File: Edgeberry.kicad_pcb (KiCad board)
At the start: 2 copper layers, 135 x 90 mm, 169 parts, among them P1 12Vin, Q1 BC547, Q2 BC547, Q3 BC547, SW1 SW_PUSH, U1 24LC256, U2 LM2596S-5.0

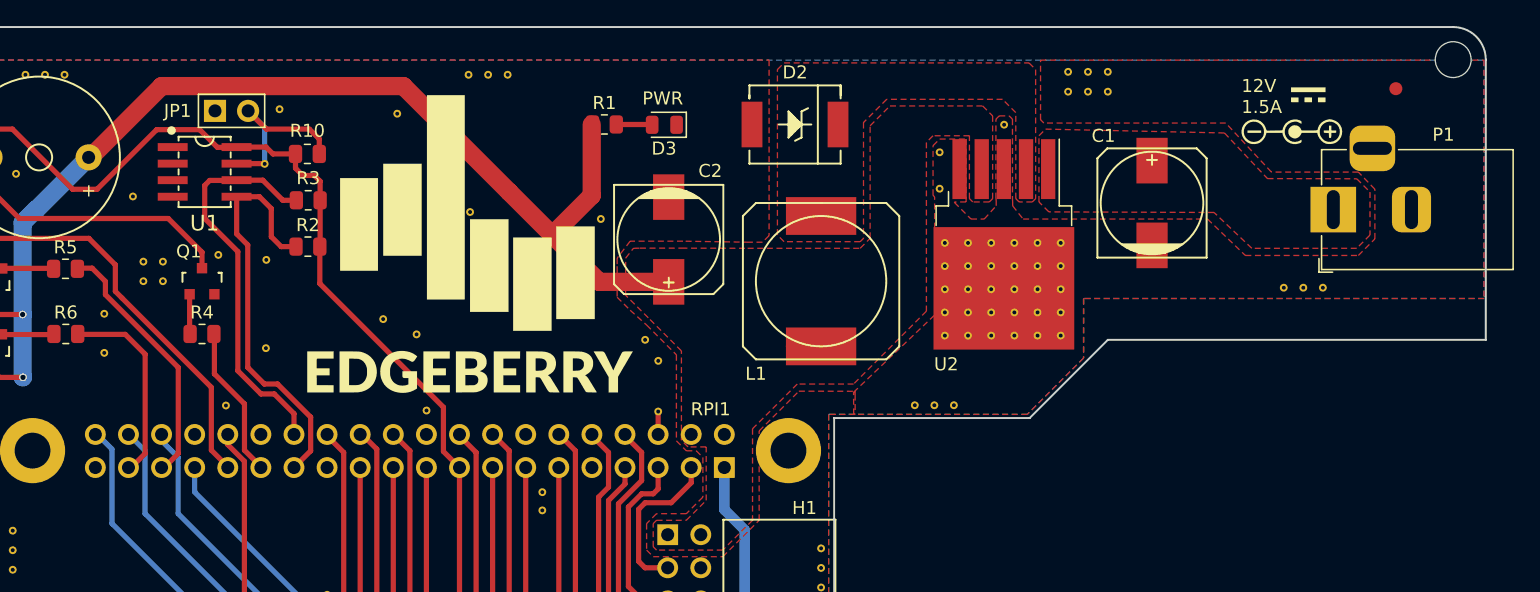
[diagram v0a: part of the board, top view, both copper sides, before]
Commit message: Added a Molex 2Pin header on 12V
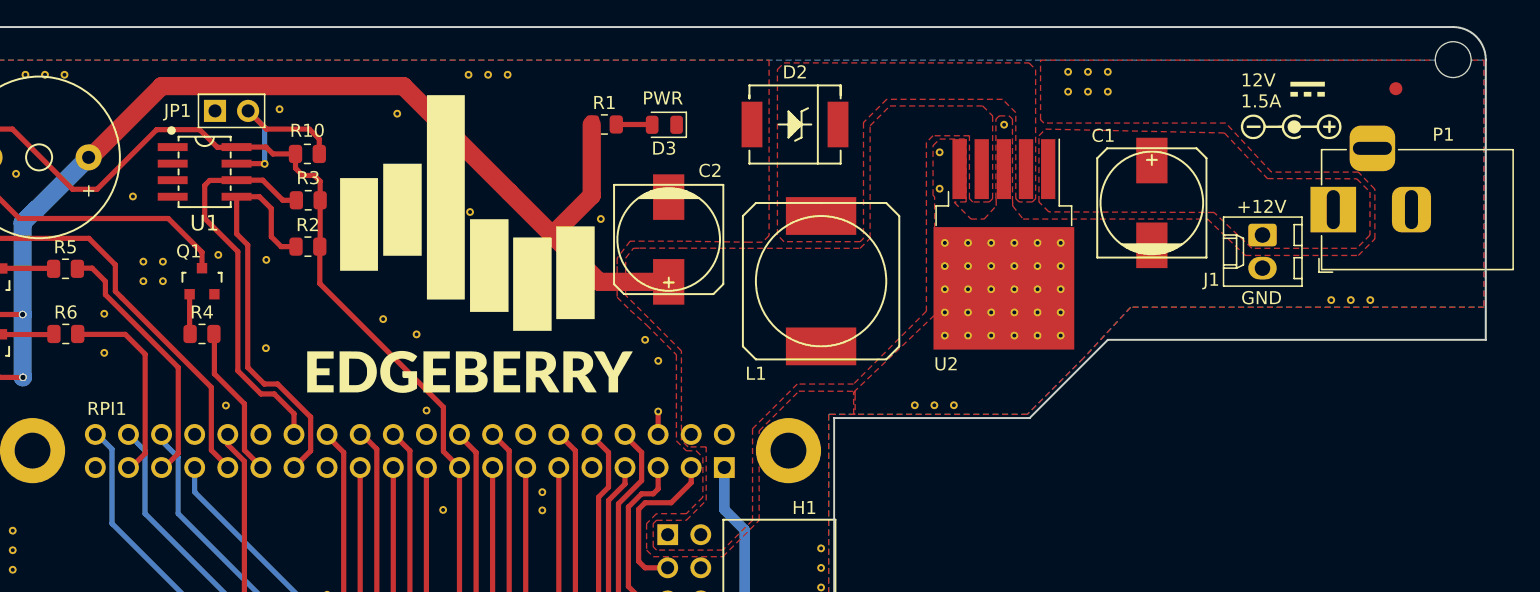
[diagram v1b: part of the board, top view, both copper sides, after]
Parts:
- added J1: Molex_KK_1x02_P2.54mm_CONN, Connector_Molex:Molex_KK-254_AE-6410-02A_1x02_P2.54mm_Vertical, F.Cu at (201.5, 67.7)
- added REF**: via_0.6mm, emcosys:via_0.6mm, B.Cu at (138.6, 88.8)
- H1: value EdgeBerry_IO -> 2X16Pin_2.54mm_Right_Angle_Receptacle_Connector
- P1: value 12Vin -> Barrel_Jack_CONN
- RPI1: value RPi_GPIO -> 2X20Pin_2.54mm_Receptacle_Connector
- moved G*** 4.80 mm to (193.4, 64.0)
- moved REF** 3.76 mm to (209.8, 72.7)
- moved REF** 3.76 mm to (208.3, 72.7)
- moved REF** 3.76 mm to (206.8, 72.7)
- moved G*** 0.43 mm to (204.9, 56.6)
- moved G*** 0.38 mm to (203.7, 59.4)
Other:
- board text added: "+12V"
- board text added: "REV 1.4"
- board text added: "REV.: 1.4, Mid 2024"
- board text removed: "REV 1.3"
- board text removed: "REV.: 1.3, Mid 2024"
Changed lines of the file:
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@@
   (net 43 "Net-(Q3-Pad2)")
   (footprint "Capacitors_SMD:c_elec_8x10" (layer "F.Cu")
-    (at 193.04 65.272 90)
+    (at 193.028 65.2672 90)
     (descr "SMT capacitor, aluminium electrolytic, 8x10")
     (property "Sheetfile" "Edgeberry.kicad_sch")
@@
       (effects (font (size 1 1) (thickness 0.15)))
     )
-    (fp_text value "EdgeBerry_IO" (at 0 -9.351 -90) (layer "F.Fab")
+    (fp_text value "2X16Pin_2.54mm_Right_Angle_Receptacle_Connector" (at 0 -4.85 -90) (layer "F.Fab")
       (effects (font (size 1 1) (thickness 0.15)))
     )
@@
     )
   )
+  (footprint "Connector_Molex:Molex_KK-254_AE-6410-02A_1x02_P2.54mm_Vertical" (layer "F.Cu")
+    (at 201.517 67.731 -90)
+    (descr "Molex KK-254 Interconnect System, old/engineering part number: AE-6410-02A example for new part number: 22-27-2021, 2 Pins (http://www.molex.com/pdm_docs/sd/022272021_sd.pdf), generated with kicad-footprint-generator")
+    (tags "connector Molex KK-254 vertical")
+    (property "Sheetfile" "Edgeberry.kicad_sch")
+    (property "Sheetname" "")
+    (attr through_hole)
+    (fp_text reference "J1" (at 3.429 3.917 180) (layer "F.SilkS")
+      (effects (font (size 1 1) (thickness 0.15)))
+    )
+    (fp_text value "Molex_KK_1x02_P2.54mm_CONN" (at 6.041 -0.02 180) (layer "F.Fab")
+      (effects (font (size 1 1) (thickness 0.15)))
+    )
+    (fp_text user "${REFERENCE}" (at 1.27 -1.732 90) (layer "F.Fab")
+      (effects (font (size 1 1) (thickness 0.15)))
+    )
+    (fp_line (start 3.34 -2.43) (end 3.34 -3.03) (layer "F.SilkS") (width 0.12))
+    (fp_line (start 2.29 1.46) (end 2.54 1.99) (layer "F.SilkS") (width 0.12))
+    (fp_line (start -1.38 2.99) (end 3.92 2.99) (layer "F.SilkS") (width 0.12))
+    (fp_line (start 0.25 1.46) (end 2.29 1.46) (layer "F.SilkS") (width 0.12))
+    (fp_line (start 3.92 2.99) (end 3.92 -3.03) (layer "F.SilkS") (width 0.12))
+    (fp_line (start 1.74 -2.43) (end 3.34 -2.43) (layer "F.SilkS") (width 0.12))
+    (fp_line (start 2.54 1.99) (end 2.54 2.99) (layer "F.SilkS") (width 0.12))
+    (fp_line (start 0 1.99) (end 2.54 1.99) (layer "F.SilkS") (width 0.12))
+    (fp_line (start 2.29 2.99) (end 2.29 1.99) (layer "F.SilkS") (width 0.12))
+    (fp_line (start 0.25 2.99) (end 0.25 1.99) (layer "F.SilkS") (width 0.12))
+    (fp_line (start 3.92 -3.03) (end -1.38 -3.03) (layer "F.SilkS") (width 0.12))
+    (fp_line (start -0.8 -2.43) (end 0.8 -2.43) (layer "F.SilkS") (width 0.12))
+    (fp_line (start 0 1.99) (end 0.25 1.46) (layer "F.SilkS") (width 0.12))
+    (fp_line (start 0 2.99) (end 0 1.99) (layer "F.SilkS") (width 0.12))
+    (fp_line (start 0.8 -2.43) (end 0.8 -3.03) (layer "F.SilkS") (width 0.12))
+    (fp_line (start -1.38 -3.03) (end -1.38 2.99) (layer "F.SilkS") (width 0.12))
+    (fp_line (start -0.8 -3.03) (end -0.8 -2.43) (layer "F.SilkS") (width 0.12))
+    (fp_line (start 1.74 -3.03) (end 1.74 -2.43) (layer "F.SilkS") (width 0.12))
+    (fp_line (start -1.77 -3.42) (end -1.77 3.38) (layer "F.CrtYd") (width 0.05))
+    (fp_line (start 4.31 -3.42) (end -1.77 -3.42) (layer "F.CrtYd") (width 0.05))
+    (fp_line (start 4.31 3.38) (end 4.31 -3.42) (layer "F.CrtYd") (width 0.05))
+    (fp_line (start -1.77 3.38) (end 4.31 3.38) (layer "F.CrtYd") (width 0.05))
+    (fp_line (start 3.81 -2.92) (end -1.27 -2.92) (layer "F.Fab") (width 0.1))
+    (fp_line (start -1.27 -0.5) (end -0.562893 0) (layer "F.Fab") (width 0.1))
+    (fp_line (start -0.562893 0) (end -1.27 0.5) (layer "F.Fab") (width 0.1))
+    (fp_line (start -1.27 -2.92) (end -1.27 2.88) (layer "F.Fab") (width 0.1))
+    (fp_line (start -1.27 2.88) (end 3.81 2.88) (layer "F.Fab") (width 0.1))
+    (fp_line (start 3.81 2.88) (end 3.81 -2.92) (layer "F.Fab") (width 0.1))
+    (pad "1" thru_hole roundrect (at 0 0 270) (size 1.74 2.19) (drill 1.19) (layers *.Cu *.Mask) (roundrect_rratio 0.143678)
+      (net 6 "+12V") (pinfunction "Pin_1") (pintype "passive"))
+    (pad "2" thru_hole oval (at 2.54 0 270) (size 1.74 2.19) (drill 1.19) (layers *.Cu *.Mask)
+      (net 2 "GND") (pinfunction "Pin_2") (pintype "passive"))
+    (model "${KICAD6_3DMODEL_DIR}/Connector_Molex.3dshapes/Molex_KK-254_AE-6410-02A_1x02_P2.54mm_Vertical.wrl"
+      (offset (xyz 0 0 -1))
+      (scale (xyz 1 1 1))
+      (rotate (xyz 0 0 90))
+    )
+    (model "/home/tom/Projects/KiCad_library/3D models/molex_kk_2.54mm_(0.1inch)_latching_2way_vertical_header.step"
+      (offset (xyz 1.2 0 1.5))
+      (scale (xyz 1 1 1))
+      (rotate (xyz -90 0 180))
+    )
+  )
   (footprint "Resistor_SMD:R_0805_2012Metric" (layer "F.Cu")
     (at 128.274 68.62 180)
@@
   )
   (footprint "LOGO" (layer "F.Cu")
-    (at 203.8 59.8)
+    (at 203.749 59.422)
     (attr board_only exclude_from_pos_files exclude_from_bom)
     (fp_text reference "G***" (at 0 0) (layer "F.SilkS") hide
@@
   )
   (footprint "LOGO" (layer "F.Cu")
-    (at 205 57)
+    (at 204.949 56.572)
     (attr board_only exclude_from_pos_files exclude_from_bom)
     (fp_text reference "G***" (at 0 0) (layer "F.SilkS") hide
@@
       (effects (font (size 1 1) (thickness 0.15)))
     )
-    (fp_text value "12Vin" (at -6.2 -5.5) (layer "F.Fab")
+    (fp_text value "Barrel_Jack_CONN" (at -6.45 -3.6425) (layer "F.Fab")
       (effects (font (size 1 1) (thickness 0.15)))
     )
-    (fp_text user "${REFERENCE}" (at -3 -2.95) (layer "F.Fab")
+    (fp_text user "${REFERENCE}" (at -2.95 -2.2425) (layer "F.Fab")
       (effects (font (size 1 1) (thickness 0.15)))
     )
@@
     (property "Sheetname" "")
     (attr through_hole)
-    (fp_text reference "RPI1" (at -23.0786 3.2035 180) (layer "F.SilkS")
+    (fp_text reference "RPI1" (at 23.2464 3.2285 180) (layer "F.SilkS")
       (effects (font (size 1 1) (thickness 0.15)))
     )
-    (fp_text value "RPi_GPIO" (at -1.9546 -3.1495 180) (layer "F.Fab")
+    (fp_text value "2X20Pin_2.54mm_Receptacle_Connector" (at -1.9546 -3.1495 180) (layer "F.Fab")
       (effects (font (size 1 1) (thickness 0.15)))
     )
@@
   )
   (footprint "emcosys:via_0.6mm" (layer "B.Cu")
-    (at 206.149 71.772 -90)
+    (at 209.792 72.722 -90)
     (attr through_hole)
     (fp_text reference "REF**" (at 0 -0.9525 -90) (layer "B.SilkS") hide
@@
   )
   (footprint "emcosys:via_0.6mm" (layer "B.Cu")
-    (at 204.649 71.772 -90)
+    (at 208.292 72.722 -90)
     (attr through_hole)
     (fp_text reference "REF**" (at 0 -0.9525 -90) (layer "B.SilkS") hide
@@
   )
   (footprint "emcosys:via_0.6mm" (layer "B.Cu")
-    (at 203.149 71.772 -90)
+    (at 206.792 72.722 -90)
     (attr through_hole)
     (fp_text reference "REF**" (at 0 -0.9525 -90) (layer "B.SilkS") hide
@@
   )
   (footprint "emcosys:via_0.6mm" (layer "B.Cu")
+    (at 138.649 88.822 -90)
+    (attr through_hole)
+    (fp_text reference "REF**" (at 0 -0.9525 -90) (layer "B.SilkS") hide
+      (effects (font (size 1 1) (thickness 0.15)) (justify mirror))
+    )
+    (fp_text value "via_0.6mm" (at 0 1.0795 -90) (layer "B.Fab") hide
+      (effects (font (size 1 1) (thickness 0.15)) (justify mirror))
+    )
+    (pad "1" thru_hole circle locked (at 0 0 270) (size 0.6 0.6) (drill 0.3) (layers *.Cu)
+      (net 2 "GND") (zone_connect 2))
+  )
+  (footprint "emcosys:via_0.6mm" (layer "B.Cu")
     (at 167.7042 125.794 -90)
     (attr through_hole)
@@
   )
   (footprint "LOGO" (layer "B.Cu")
-    (at 198.249 63.972 180)
+    (at 193.449 63.972 180)
     (attr board_only exclude_from_pos_files exclude_from_bom)
     (fp_text reference "G***" (at 0 0) (layer "F.SilkS") hide
@@
     (effects (font (size 1 1) (thickness 0.25)) (justify right mirror))
   )
-  (gr_text "REV 1.3" (at 130.7218 69.636) (layer "B.SilkS")
+  (gr_text "REV 1.4" (at 130.7218 69.636) (layer "B.SilkS")
     (effects (font (size 1.5 1.5) (thickness 0.3)) (justify mirror))
   )
@@
     (effects (font (size 1 1) (thickness 0.25)) (justify right mirror))
   )
-  (gr_text "MORE INFO ON" (at 198.149 57.772) (layer "B.SilkS")
+  (gr_text "MORE INFO ON" (at 193.449 57.772) (layer "B.SilkS")
     (effects (font (size 1 0.95) (thickness 0.15)) (justify mirror))
   )
@@
     (effects (font (size 1 1) (thickness 0.25)) (justify right mirror))
   )
-  (gr_text "EDGEBERRY.IO" (at 198.149 70.272) (layer "B.SilkS")
+  (gr_text "EDGEBERRY.IO" (at 193.449 70.272) (layer "B.SilkS")
     (effects (font (size 1 1) (thickness 0.15)) (justify mirror))
   )
@@
     (effects (font (size 1 1) (thickness 0.25)) (justify left mirror))
   )
-  (gr_text "12V\n1.5A" (at 199.9 57.1) (layer "F.SilkS")
+  (gr_text "GND" (at 201.449 72.572) (layer "F.SilkS")
+    (effects (font (size 1 1) (thickness 0.25)))
+  )
+  (gr_text "12V\n1.5A" (at 199.849 56.672) (layer "F.SilkS")
     (effects (font (size 1 1) (thickness 0.2)) (justify left))
   )
@@
     (effects (font (size 1.45 1.45) (thickness 0.3625)) (justify left))
   )
+  (gr_text "+12V" (at 201.449 65.572) (layer "F.SilkS")
+    (effects (font (size 1 1) (thickness 0.25)))
+  )
   (gr_text "PWR" (at 155.5 57.25) (layer "F.SilkS")
     (effects (font (size 1 1) (thickness 0.2)))
@@
     (effects (font (size 0.55 0.55) (thickness 0.125)) (justify left))
   )
-  (gr_text "Raspberry Pi" (at 137.249 135.636) (layer "Dwgs.User")
+  (gr_text "Raspberry Pi" (at 115.999 87.472) (layer "Dwgs.User")
     (effects (font (size 1 1) (thickness 0.15)))
   )
@@
     (effects (font (size 5 5) (thickness 1)) (justify left))
   )
-  (gr_text "REV.: 1.3, Mid 2024" (at 179 178.75) (layer "Dwgs.User")
+  (gr_text "REV.: 1.4, Mid 2024" (at 179 178.75) (layer "Dwgs.User")
     (effects (font (size 2 2) (thickness 0.3)) (justify left))
   )
@@
     (polygon
       (pts
-        (xy 218.523 72.6)
-        (xy 187.789 72.6)
+        (xy 218.523 73.272)
+        (xy 191.399 73.272)
         (xy 187.789 77.172)
         (xy 183.471 81.49)
@@
       (pts
         (xy 218.523 54.312)
-        (xy 218.523 72.6)
-        (xy 187.789 72.6)
+        (xy 218.523 73.272)
+        (xy 191.399 73.272)
         (xy 187.789 77.172)
         (xy 183.471 81.49)
